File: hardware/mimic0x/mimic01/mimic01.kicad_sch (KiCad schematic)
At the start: 33 parts, among them J2 Conn_01x06, J3 Conn_01x03, J5 Conn_01x05, Q1 AO3401A, SW1 TS-1088-AR02016, U1 PY32F071C1BU6TR_DIY

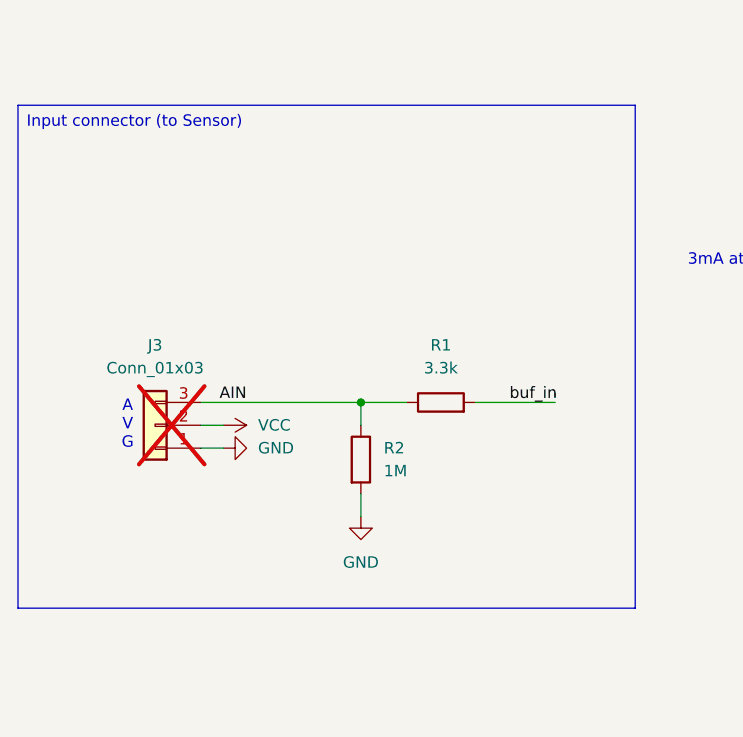
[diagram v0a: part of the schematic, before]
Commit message: change input bias voltage
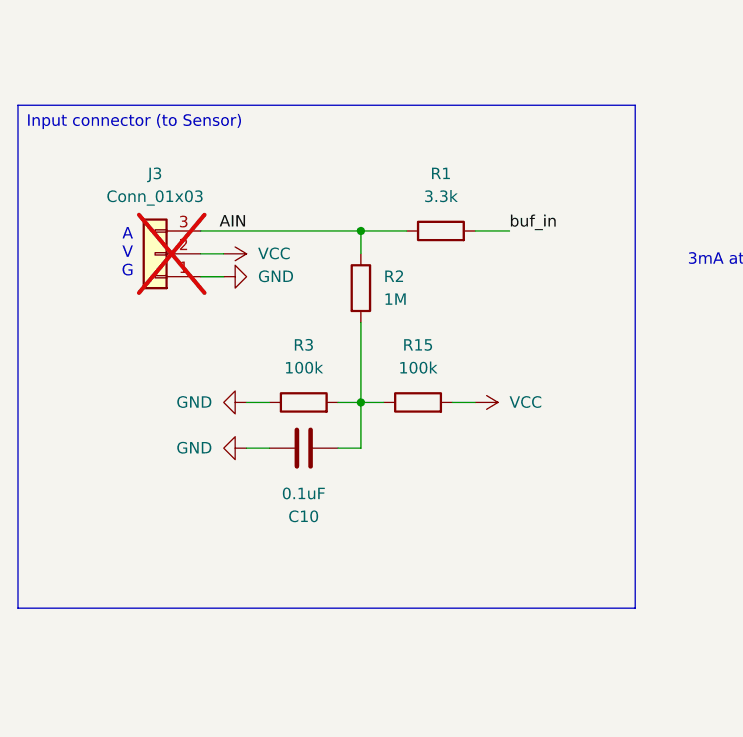
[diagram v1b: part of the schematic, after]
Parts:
- added C10: 0.1uF, Capacitor_SMD:C_0402_1005Metric, symbol Device:C
- added R15, R3: 100k, Resistor_SMD:R_0402_1005Metric, symbol Device:R
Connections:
- net GND: now also C10.2, R3.1; no longer R2.2
- net VCC: now also R15.2
- new net: C10.1, R15.1, R2.2, R3.2
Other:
- moved on the sheet: J3, R1, R2

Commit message: add input bias, vdd/2
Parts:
- R11, R12, R13: value 3.3k -> 10k; LCSC Part C25890 -> C25744
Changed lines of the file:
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@@
 			)
 		)
-		(property "Value" "3.3k"
+		(property "Value" "10k"
 			(at 157.48 149.8599 0)
 			(show_name no)
@@
 			)
 		)
-		(property "LCSC Part" "C25890"
+		(property "LCSC Part" "C25744"
 			(at 154.94 148.59 0)
 			(hide yes)
@@
 			)
 		)
-		(property "Value" "3.3k"
+		(property "Value" "10k"
 			(at 149.86 149.8599 0)
 			(show_name no)
@@
 			)
 		)
-		(property "LCSC Part" "C25890"
+		(property "LCSC Part" "C25744"
 			(at 147.32 148.59 0)
 			(hide yes)
@@
 			)
 		)
-		(property "Value" "3.3k"
+		(property "Value" "10k"
 			(at 166.37 137.1599 0)
 			(show_name no)
@@
 			)
 		)
-		(property "LCSC Part" "C25890"
+		(property "LCSC Part" "C25744"
 			(at 163.83 135.89 0)
 			(hide yes)
